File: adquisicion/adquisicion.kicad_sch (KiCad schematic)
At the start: 34 parts, among them J1 Coax Antena 1, J2 Coax Antena 2, J3 Screw_Terminal_01x04, J5 Conn_01x08_Socket, J6 Conn_01x15_Pin, J7 Conn_01x10_Socket, U2 L7805, U3 YAAJ_BluePill_Part_Like

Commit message: Mejoras layout, corrección ERC y DRC
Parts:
- added R7: 0, huellas_proyecto:R_Axial_DIN0207_L6.3mm_D2.5mm_P15.24mm_Horizontal-pad2mm, symbol Device:R
- U3: footprint Footprints:YAAJ_BluePill_2 -> huellas_proyecto:YAAJ_BluePill_2; symbol YAAJ_BluePill_Part_Like:YAAJ_BluePill_Part_Like -> simbolos_proyecto:YAAJ_BluePill_Part_Like
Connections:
- net Reset: now also R7.2; no longer U3.37 (RST)
- new net: R7.1, U3.37 (RST)
- no-connect marks 40 -> 56
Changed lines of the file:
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@@
 	)
 	(no_connect
+		(at 184.15 129.54)
+	)
+	(no_connect
 		(at 207.01 55.88)
 	)
@@
 	)
 	(no_connect
+		(at 184.15 134.62)
+	)
+	(no_connect
+		(at 184.15 137.16)
+	)
+	(no_connect
 		(at 207.01 48.26)
 	)
@@
 	)
 	(no_connect
+		(at 184.15 121.92)
+	)
+	(no_connect
 		(at 152.4 121.92)
 	)
@@
 	)
 	(no_connect
+		(at 184.15 106.68)
+	)
+	(no_connect
 		(at 207.01 83.82)
 	)
 	(no_connect
+		(at 184.15 119.38)
+	)
+	(no_connect
 		(at 207.01 50.8)
 	)
 	(no_connect
+		(at 184.15 139.7)
+	)
+	(no_connect
+		(at 184.15 111.76)
+	)
+	(no_connect
 		(at 152.4 147.32)
 	)
@@
 	)
 	(no_connect
+		(at 184.15 147.32)
+	)
+	(no_connect
 		(at 166.37 55.88)
 	)
@@
 	)
 	(no_connect
+		(at 184.15 144.78)
+	)
+	(no_connect
 		(at 166.37 73.66)
 	)
@@
 	)
 	(no_connect
+		(at 184.15 152.4)
+	)
+	(no_connect
 		(at 207.01 60.96)
 	)
 	(no_connect
+		(at 184.15 142.24)
+	)
+	(no_connect
 		(at 152.4 137.16)
 	)
@@
 	)
 	(no_connect
+		(at 184.15 127)
+	)
+	(no_connect
 		(at 207.01 81.28)
 	)
@@
 	)
 	(no_connect
+		(at 184.15 149.86)
+	)
+	(no_connect
 		(at 152.4 119.38)
 	)
 	(no_connect
+		(at 184.15 116.84)
+	)
+	(no_connect
 		(at 166.37 86.36)
 	)
@@
 	)
 	(no_connect
+		(at 184.15 109.22)
+	)
+	(no_connect
 		(at 166.37 78.74)
 	)
@@
 	(wire
 		(pts
+			(xy 219.71 45.72) (xy 226.06 45.72)
+		)
+		(stroke
+			(width 0)
+			(type default)
+		)
+	)
+	(wire
+		(pts
 			(xy 114.3 36.83) (xy 106.68 36.83)
 		)
@@
 	(wire
 		(pts
-			(xy 63.5 34.29) (xy 67.31 34.29)
+			(xy 207.01 45.72) (xy 212.09 45.72)
 		)
 		(stroke
@@
 	(wire
 		(pts
-			(xy 106.68 26.67) (xy 114.3 26.67)
+			(xy 63.5 34.29) (xy 67.31 34.29)
 		)
 		(stroke
@@
 	(wire
 		(pts
-			(xy 207.01 38.1) (xy 207.01 39.37)
+			(xy 106.68 26.67) (xy 114.3 26.67)
 		)
 		(stroke
@@
 	(wire
 		(pts
-			(xy 207.01 45.72) (xy 218.44 45.72)
+			(xy 207.01 38.1) (xy 207.01 39.37)
 		)
 		(stroke
@@
 	(global_label "Reset"
 		(shape input)
-		(at 218.44 45.72 0)
+		(at 226.06 45.72 0)
 		(fields_autoplaced yes)
 		(effects
@@
 		)
 		(property "Intersheetrefs" "${INTERSHEET_REFS}"
-			(at 226.6262 45.72 0)
+			(at 234.2462 45.72 0)
 			(effects
 				(font
@@
 	)
 	(symbol
-		(lib_id "YAAJ_BluePill_Part_Like:YAAJ_BluePill_Part_Like")
+		(lib_id "simbolos_proyecto:YAAJ_BluePill_Part_Like")
 		(at 186.69 60.96 0)
 		(unit 1)
@@
 			)
 		)
-		(property "Footprint" "Footprints:YAAJ_BluePill_2"
+		(property "Footprint" "huellas_proyecto:YAAJ_BluePill_2"
 			(at 204.47 86.36 0)
 			(effects
@@
 					(unit 1)
 				)
+			)
+		)
+	)
+	(symbol
+		(lib_id "Device:R")
+		(at 215.9 45.72 90)
+		(unit 1)
+		(exclude_from_sim no)
+		(in_bom yes)
+		(on_board yes)
+		(dnp no)
+		(property "Reference" "R7"
+			(at 213.106 48.006 90)
+			(effects
+				(font
+					(size 1.27 1.27)
+				)
+			)
+		)
+		(property "Value" "0"
+			(at 215.9 48.006 90)
+			(effects
+				(font
+					(size 1.27 1.27)
+				)
+			)
+		)
+		(property "Footprint" "huellas_proyecto:R_Axial_DIN0207_L6.3mm_D2.5mm_P15.24mm_Horizontal-pad2mm"
+			(at 215.9 47.498 90)
+			(effects
+				(font
+					(size 1.27 1.27)
+				)
+				(hide yes)
+			)
+		)
+		(property "Datasheet" "~"
+			(at 215.9 45.72 0)
+			(effects
+				(font
+					(size 1.27 1.27)
+				)
+				(hide yes)
+			)
+		)
+		(property "Description" "Resistor"
+			(at 215.9 45.72 0)
+			(effects
+				(font
+					(size 1.27 1.27)
+				)
+				(hide yes)
+			)
+		)
+		(pin "1"
+		)
+		(pin "2"
+		)
+		(instances
+			(project ""
+				(path "/af45896c-7063-4800-abc6-a11933bf4552"
+					(reference "R7")
+					(unit 1)
+				)

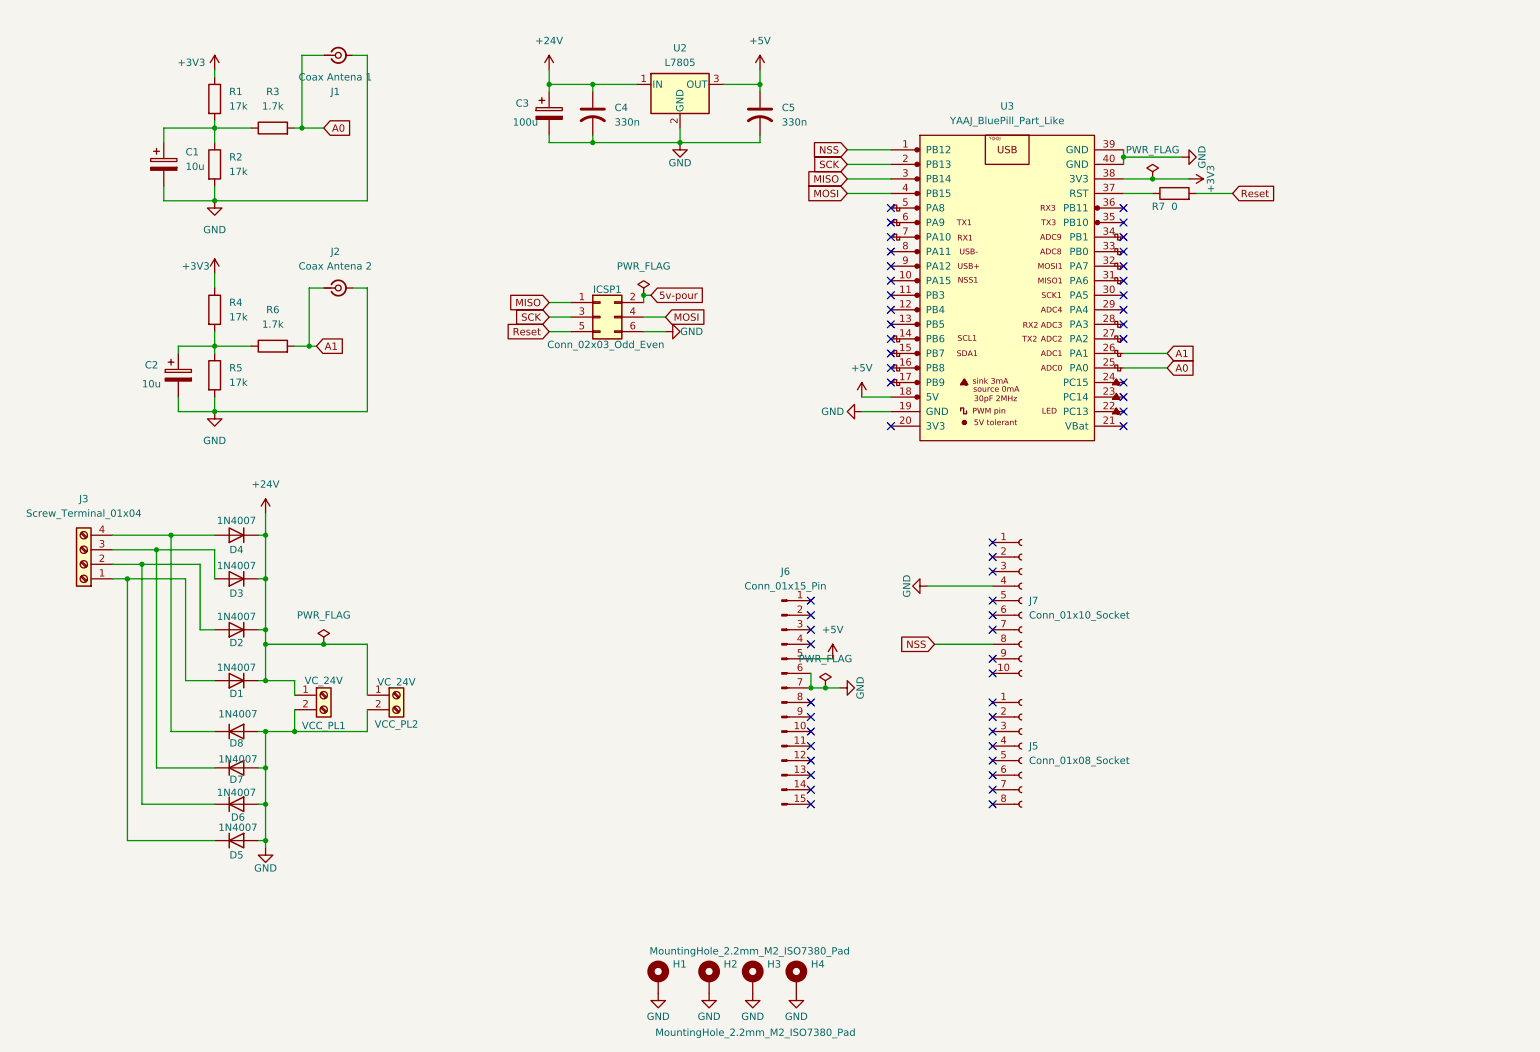
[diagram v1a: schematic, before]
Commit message: Modificación posición C5 C6 en placa Acondicionador y cambio de huella sma (verificar), cambio de huella sma en placa Adquisición (verificar)
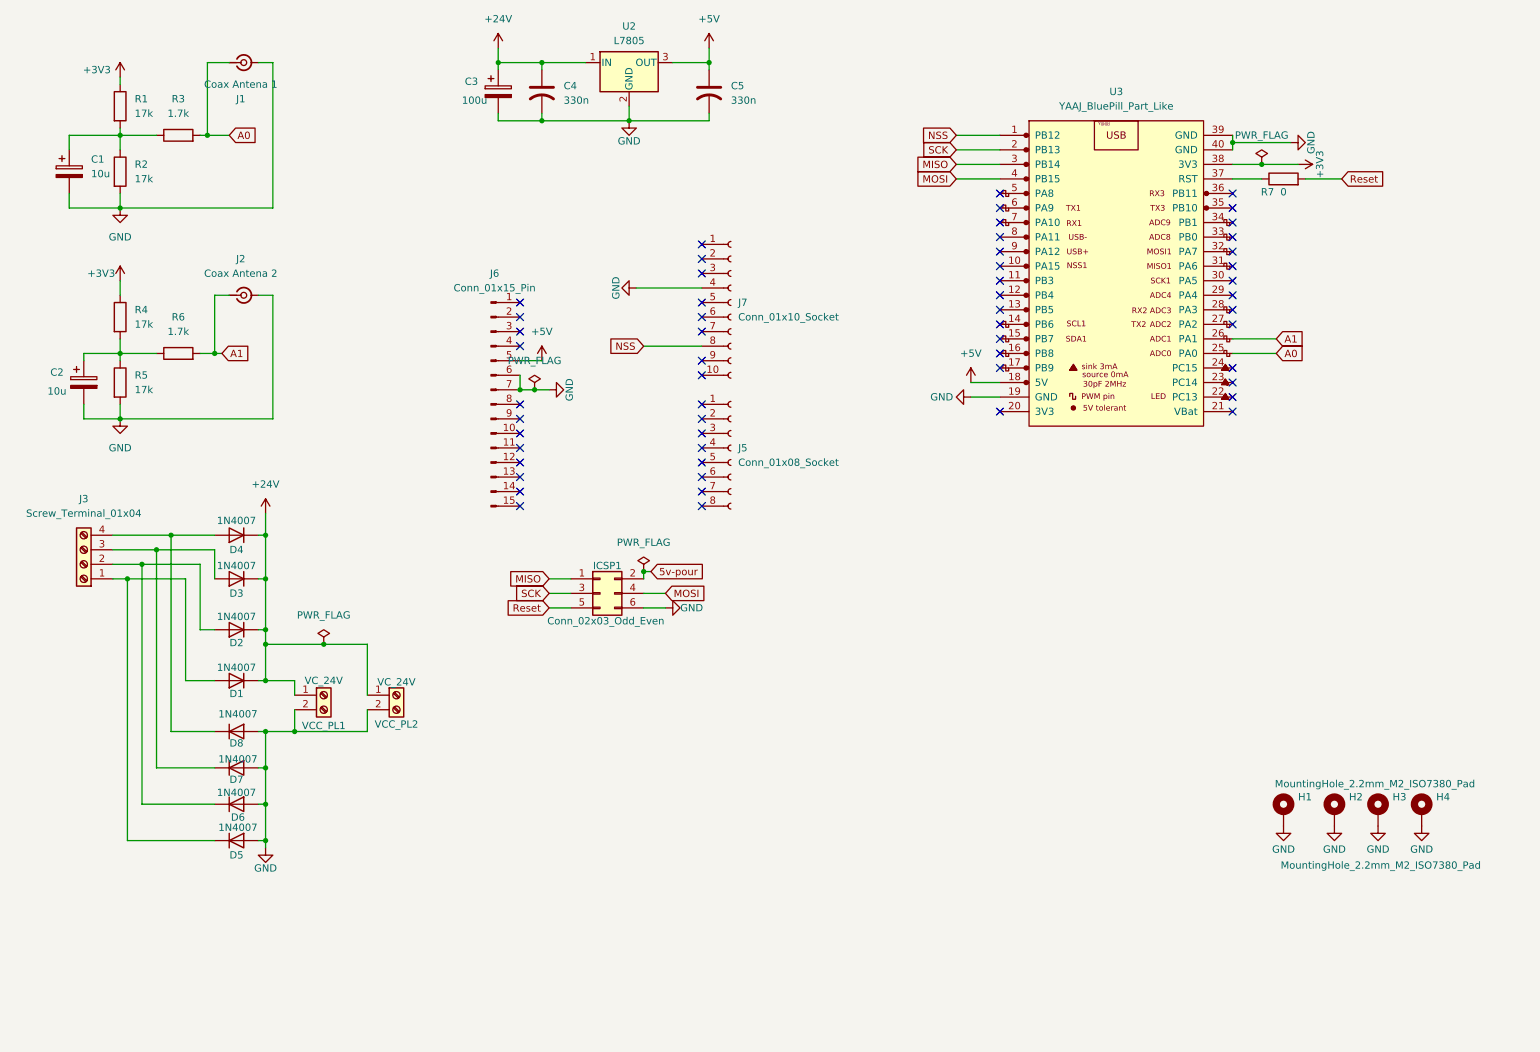
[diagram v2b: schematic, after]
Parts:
- J1, J2: footprint Connector_Coaxial:SMA_Amphenol_132289_EdgeMount -> Connector_Coaxial:SMA_Samtec_SMA-J-P-H-ST-EM1_EdgeMount
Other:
- moved on the sheet: C1, C2, C3, C4, C5, H1, H2, H3, H4, ICSP1, J1, J2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
